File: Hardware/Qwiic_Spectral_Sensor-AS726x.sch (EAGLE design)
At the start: 31 parts, among them J1 Qwiic Right Angle, J2 Serial Interface, J4 Qwiic Right Angle, J5 Flash Programming, U1 IR, U3 4MB Flash

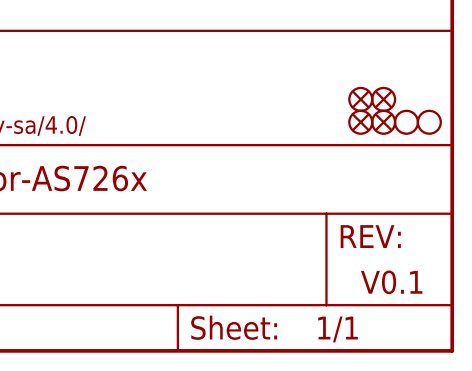
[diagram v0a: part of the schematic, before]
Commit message: Changed version number to match SFE style
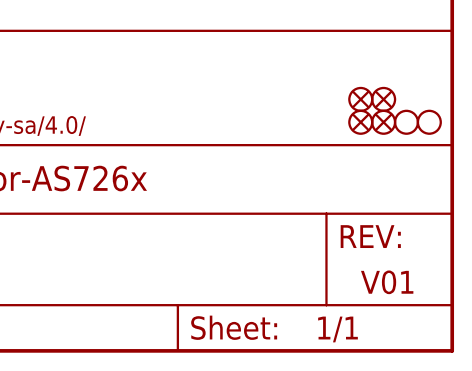
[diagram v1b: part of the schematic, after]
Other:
- note added: "V01"
- note removed: "V0.1"
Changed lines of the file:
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@@
 <text x="11.938" y="56.134" size="1.27" layer="97" rot="R180" align="center-right">Clear JP1 to remove
 I2C pullups from bus</text>
-<text x="238.76" y="7.62" size="2.54" layer="94" align="center-left">V0.1</text>
+<text x="238.76" y="7.62" size="2.54" layer="94" align="center-left">V01</text>
 <text x="170.688" y="12.446" size="2.54" layer="94" align="center-left">Nathan Seidle</text>
 <wire x1="0" y1="76.2" x2="129.54" y2="76.2" width="0.2032" layer="97" style="longdash"/>

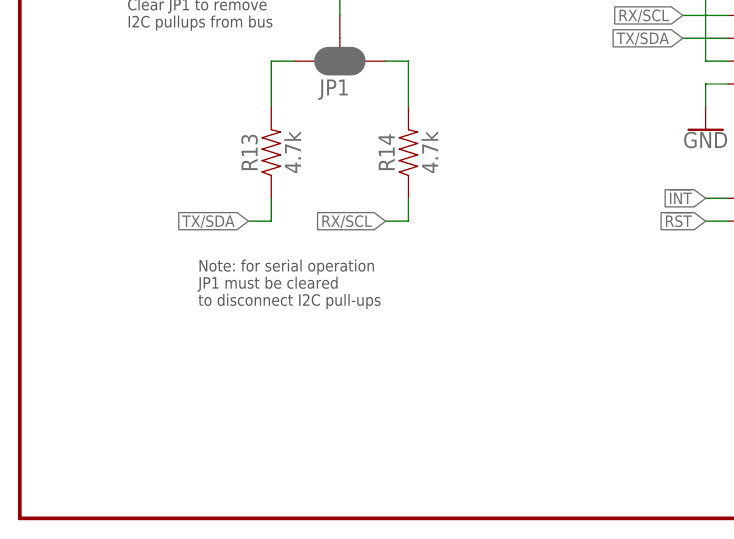
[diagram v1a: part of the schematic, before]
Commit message: Added non default constructor, License in wrong place
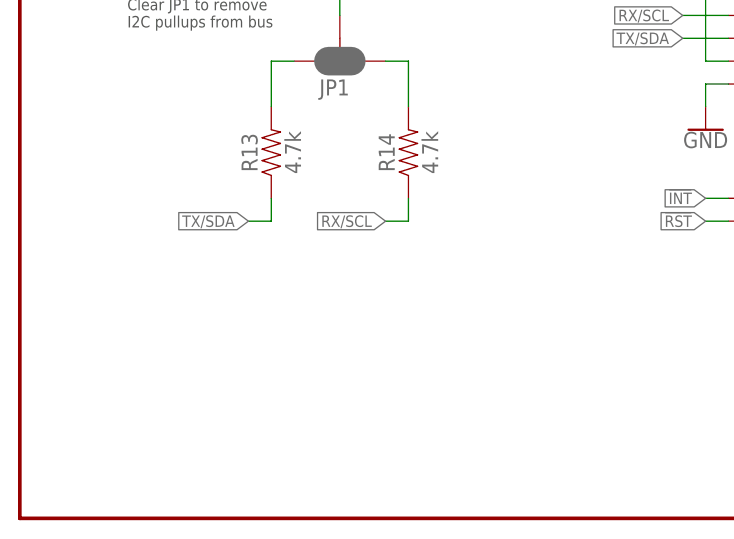
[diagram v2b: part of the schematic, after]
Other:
- note removed: "Note: for serial operation JP1 must be cleared to disconnect I2C pull-ups"
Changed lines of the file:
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@@
 <text x="170.942" y="170.942" size="2.54" layer="94" rot="MR180" align="top-left">4mbit Flash Memory</text>
 <text x="120.142" y="69.342" size="2.54" layer="94" rot="MR180" align="top-left">Interfaces</text>
-<text x="19.812" y="23.622" size="1.27" layer="97" ratio="15">Note: for serial operation
-JP1 must be cleared
-to disconnect I2C pull-ups </text>
 <text x="149.352" y="97.282" size="1.778" layer="97">The AS726x must be held in reset while programming flash</text>
 <text x="43.18" y="160.02" size="1.27" layer="97" align="center-left">Open JP4 to use an external bulb</text>

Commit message: Changed version number
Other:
- note added: "V10"
- note removed: "V01"
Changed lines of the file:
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@@
 <text x="11.938" y="56.134" size="1.27" layer="97" rot="R180" align="center-right">Clear JP1 to remove
 I2C pullups from bus</text>
-<text x="238.76" y="7.62" size="2.54" layer="94" align="center-left">V01</text>
+<text x="238.76" y="7.62" size="2.54" layer="94" align="center-left">V10</text>
 <text x="170.688" y="12.446" size="2.54" layer="94" align="center-left">Nathan Seidle</text>
 <wire x1="0" y1="76.2" x2="129.54" y2="76.2" width="0.2032" layer="97" style="longdash"/>
